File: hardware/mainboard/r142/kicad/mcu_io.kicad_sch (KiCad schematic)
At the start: 43 parts, among them J2 Hirose DM3AT-SF-PEJM5, SW2 BOOT / RECOVERY, SW3 TL1016AAF160QG, SW4 TL1016AAF160QG, SW5 TL1016AAF160QG, SW6 TL1016AAF160QG, U1 ESP32-S3-WROOM-1-N16R8, U10 TLV3012BIDBVR, U11 TLV803EA30DBZR, U5 BMI270, U9 TMUX1101DBVR

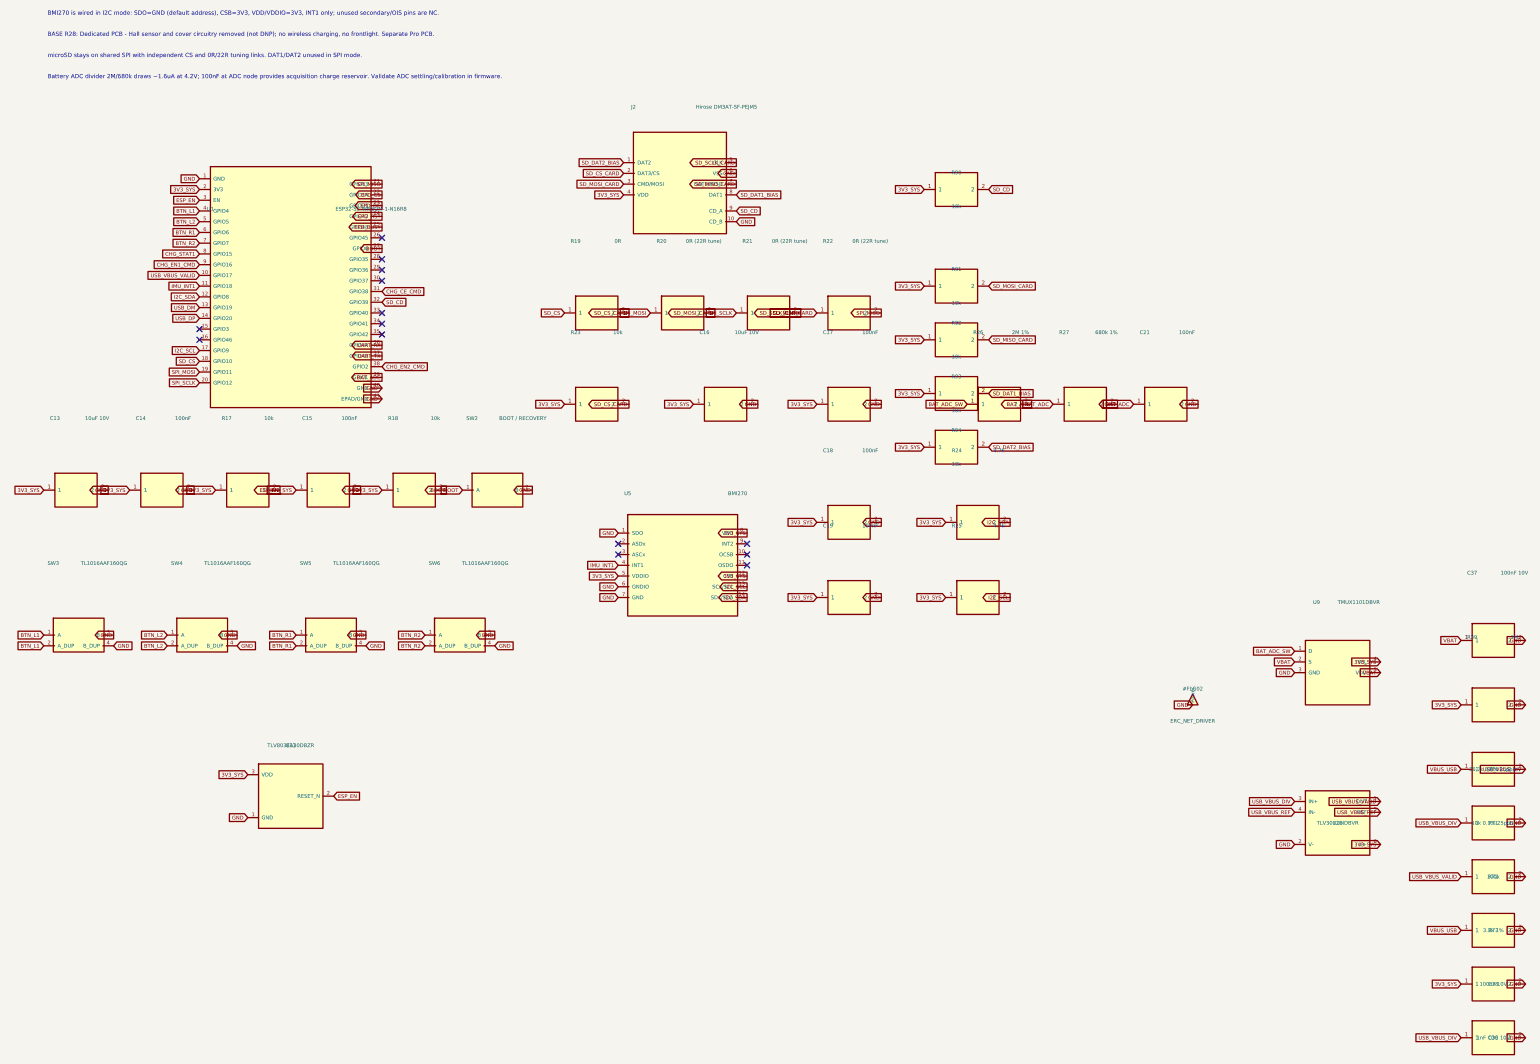
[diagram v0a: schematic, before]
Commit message: R142: separate SD schematic group and refresh engineering notes; preserve electrical graph
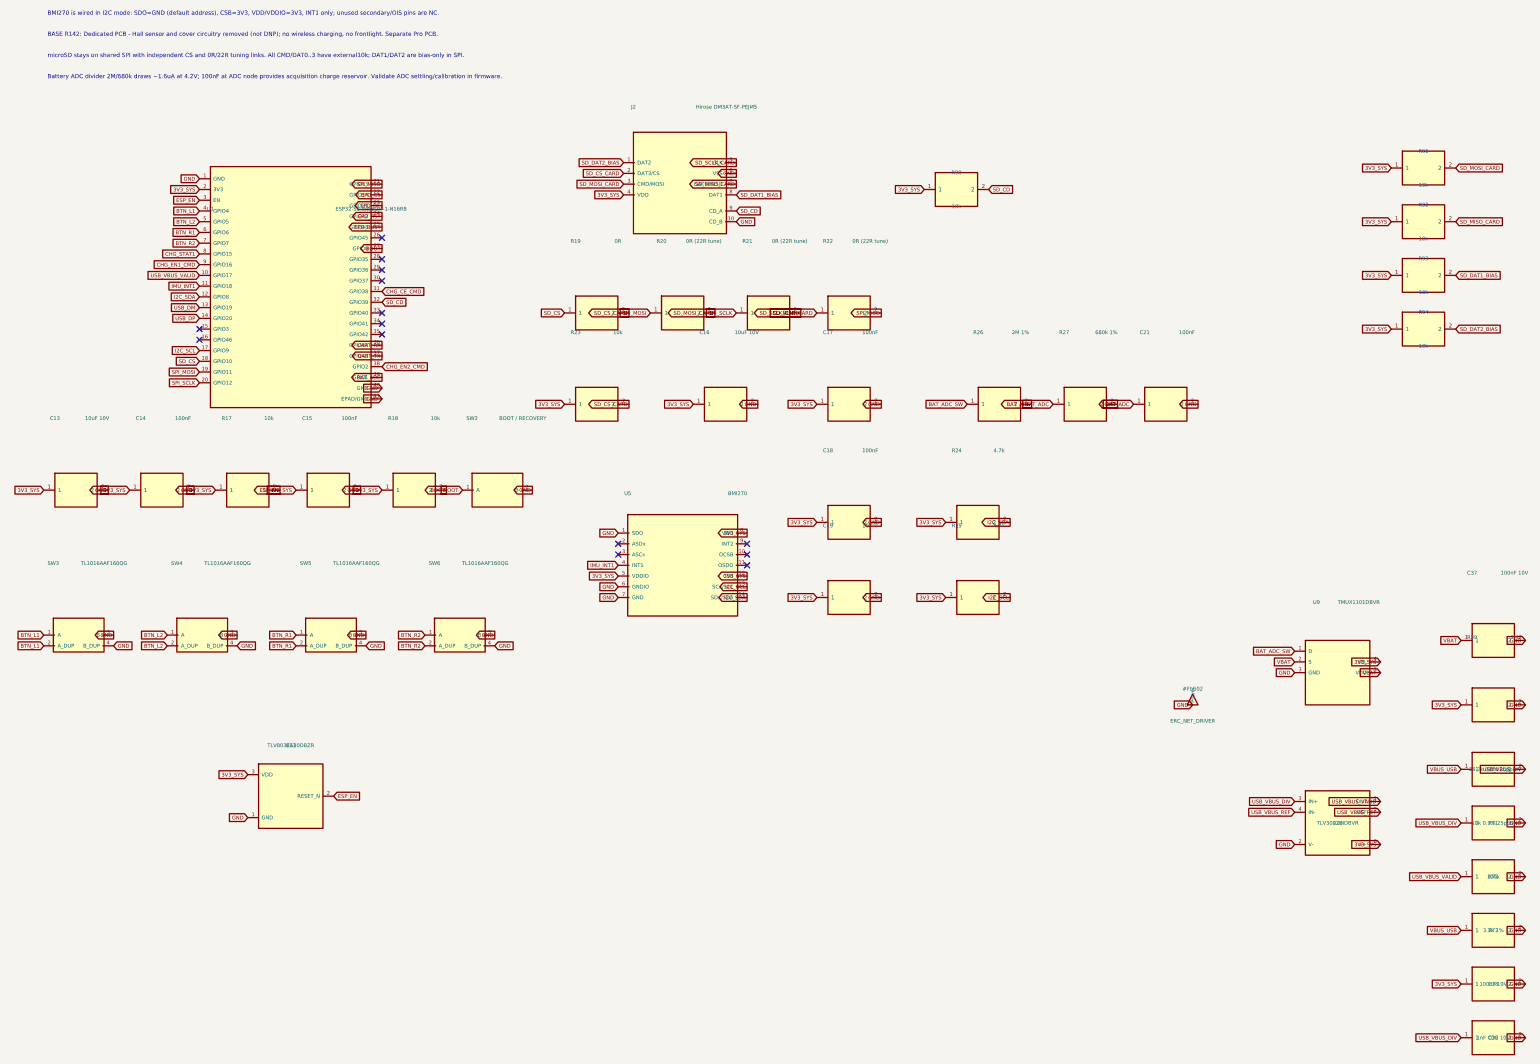
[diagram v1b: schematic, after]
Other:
- note added: "BASE R142: Dedicated PCB - Hall sensor and cover circuitry removed (not DNP); no wireless charging, no frontlight. Separate Pro PCB."
- note added: "microSD stays on shared SPI with independent CS and 0R/22R tuning links. All CMD/DAT0..3 have external10k; DAT1/DAT2 are bias-only in SPI."
- note removed: "BASE R28: Dedicated PCB - Hall sensor and cover circuitry removed (not DNP); no wireless charging, no frontlight. Separate Pro PCB."
- note removed: "microSD stays on shared SPI with independent CS and 0R/22R tuning links. DAT1/DAT2 unused in SPI mode."
- moved on the sheet: R91, R92, R93, R94
